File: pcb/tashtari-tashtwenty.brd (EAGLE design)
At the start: 26 x 33 mm, 40 parts

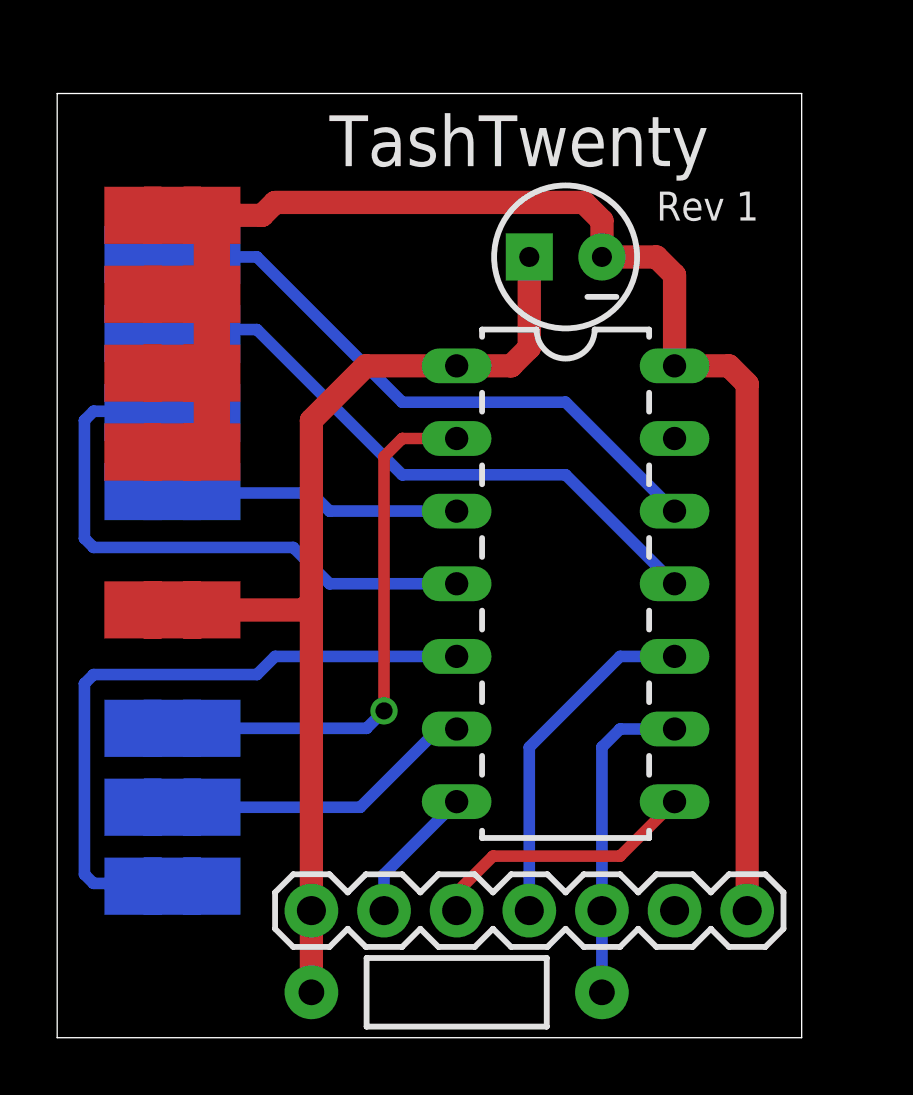
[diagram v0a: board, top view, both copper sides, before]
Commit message: add list of PCBs/products to README
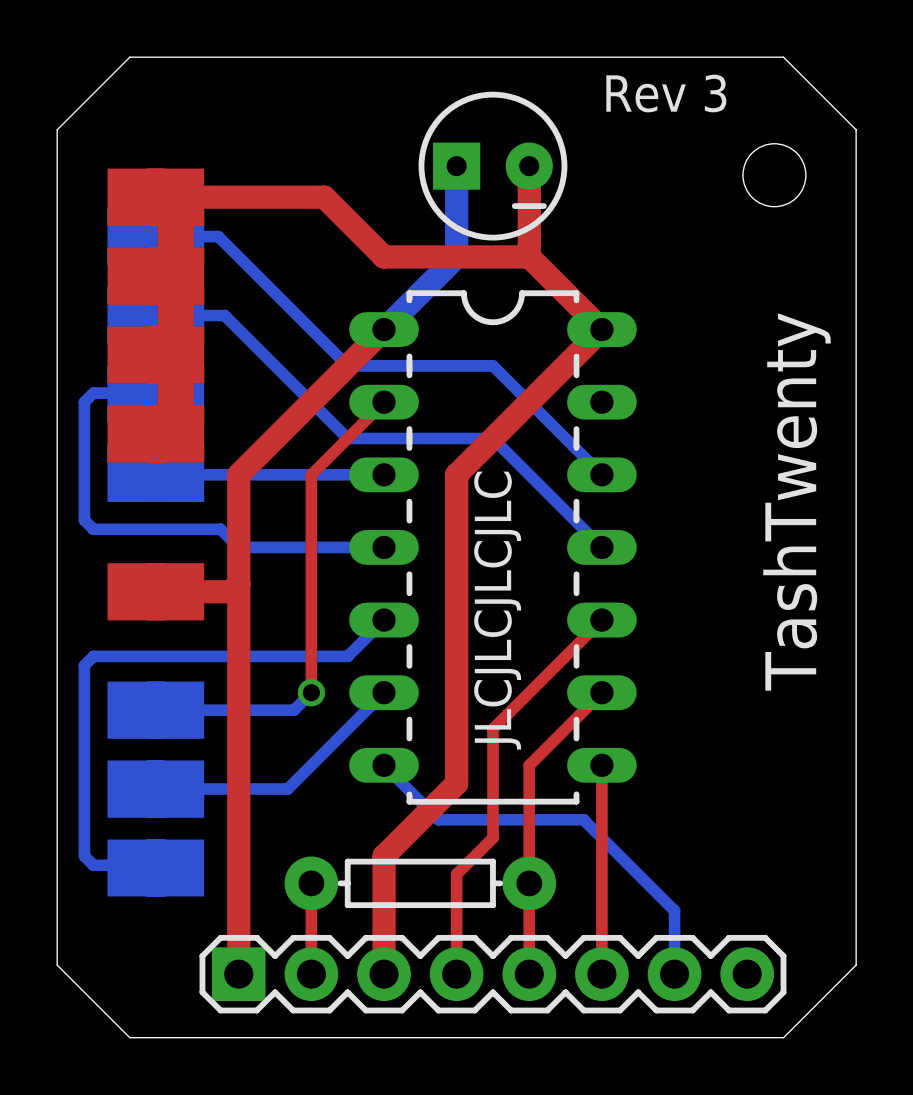
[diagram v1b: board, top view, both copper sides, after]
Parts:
- removed E$1, E$16, E$17, E$2, E$20, E$23, E$26, E$29, E$30, E$5, E$6, E$7: (no value), testpad:TP20SQ
- E$38: device SparkFun-Connectors:1X07 -> SparkFun-Connectors:1X08
- E$40: device SparkFun-Passives:AXIAL-0.4 -> SparkFun-Resistors:AXIAL-0.3
- moved E$39 4.07 mm to (15.2, 30.5)
- moved E$40 4.02 mm to (12.7, 5.40)
- moved E$38 3.38 mm to (6.35, 2.22)
- moved E$37 2.84 mm to (15.2, 15.9)
- moved E$10 1.42 mm to (2.76, 26.6)
- moved E$11 1.42 mm to (4.14, 26.6)
- moved E$12 1.42 mm to (2.76, 23.9)
- moved E$13 1.42 mm to (4.14, 23.9)
- moved E$18 1.42 mm to (2.76, 28.0)
- moved E$19 1.42 mm to (4.14, 28.0)
- moved E$24 1.42 mm to (2.76, 22.5)
- moved E$25 1.42 mm to (4.14, 22.5)
- moved E$14 1.42 mm to (4.14, 15.6)
- moved E$15 1.42 mm to (2.76, 15.6)
- moved E$31 1.42 mm to (2.76, 5.93)
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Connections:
- new net S$14: E$38.2, E$40.P$1
- net S$1: no longer E$40.P$1
- net S$2: now also E$38.3; no longer E$38.7
- net S$3: now also E$38.7; no longer E$38.2
- net S$4: now also E$38.6; no longer E$38.3
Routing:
- net S$3: track 4.86 -> 14.5 mm
- net S$11: track 22.8 -> 18.7 mm
- net S$7: track 24.7 -> 21.2 mm
- net S$14: track 0.00 -> 3.17 mm
- net S$2: track 50.8 -> 54.0 mm
- net S$5: track 12.1 -> 14.5 mm
- net S$4: track 9.57 -> 7.30 mm
- net S$9: track 18.0 -> 16.2 mm
- net S$1: track 35.4 -> 33.7 mm
- net S$12: track 19.9 -> 18.3 mm
- net S$10: track 8.84 -> 7.31 mm
- net S$13: track 19.9 -> 18.4 mm
- net S$8: track 9.69 -> 8.69 mm
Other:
- board size 26 x 33 mm -> 27.9 x 34.3 mm
- board text added: "JLCJLCJLCJLC"
- board text added: "Rev 3"
- board text removed: "Rev 1"
